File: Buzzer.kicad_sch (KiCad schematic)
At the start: 6 parts, among them Q2 MMBT3904

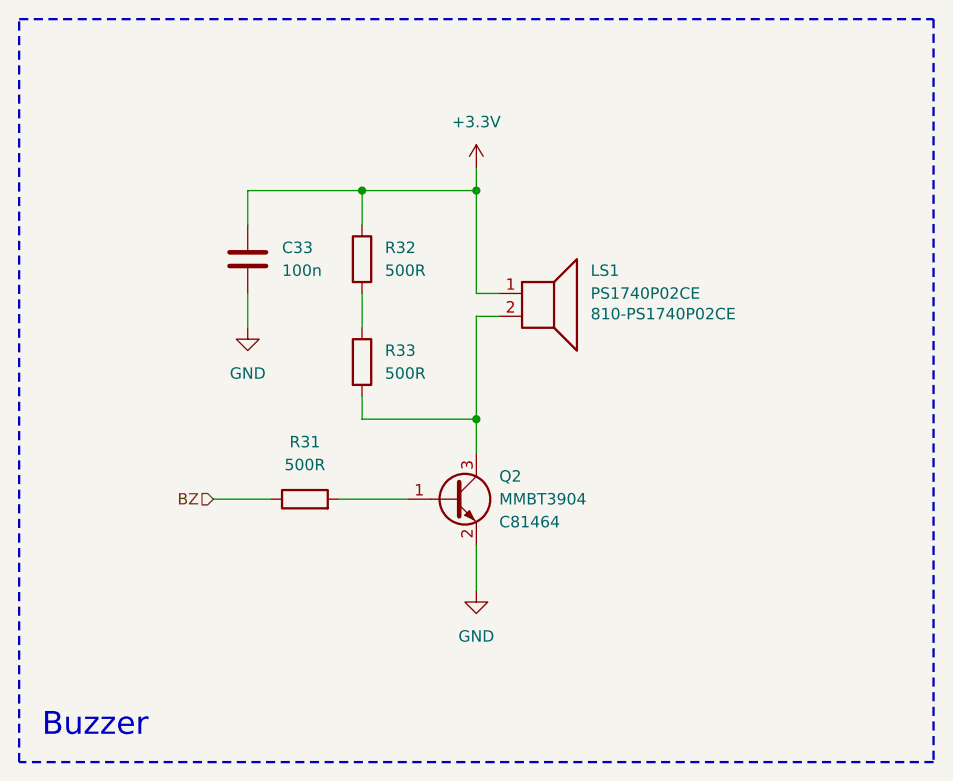
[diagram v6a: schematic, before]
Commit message: display driver update
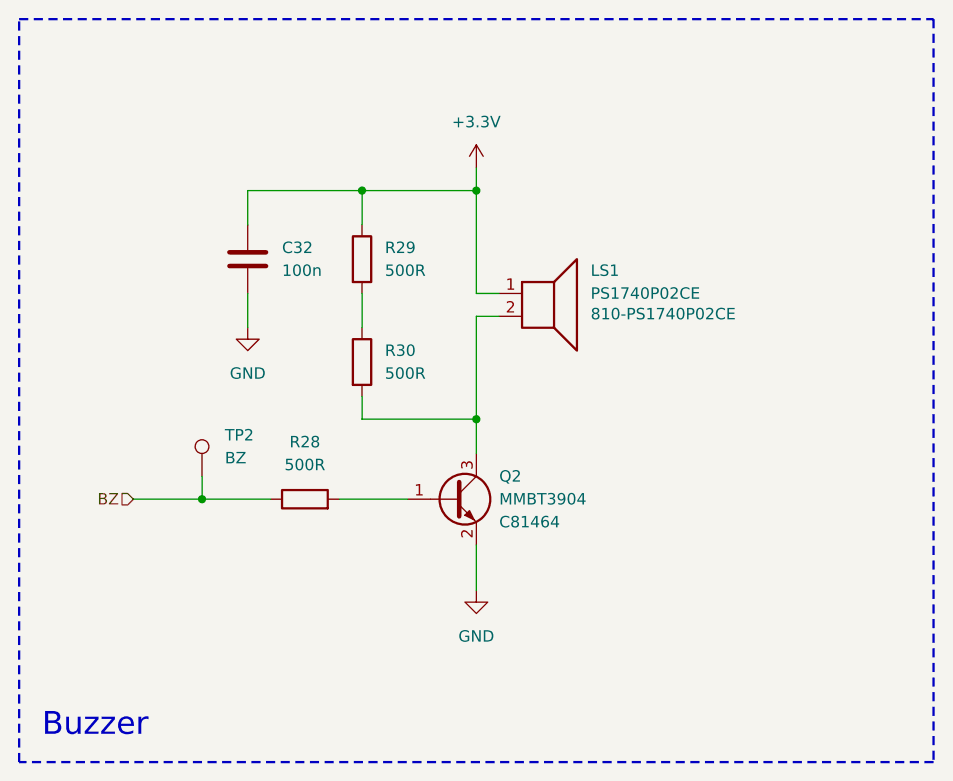
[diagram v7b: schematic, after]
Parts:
- added TP2: BZ, TestPoint:TestPoint_Pad_D1.0mm, symbol Connector:TestPoint
- renumbered C33 to C32, R31 to R28, R32 to R29, R33 to R30
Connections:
- net BZ: now also TP2.1
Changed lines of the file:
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@@
+	)
+	(junction
+		(at 121.92 110.49)
+		(diameter 0)
+		(color 0 0 0 0)
 	)
 	(junction
@@
 	(wire
 		(pts
+			(xy 121.92 107.95) (xy 121.92 110.49)
+		)
+		(stroke
+			(width 0)
+			(type default)
+		)
+	)
+	(wire
+		(pts
 			(xy 154.94 87.63) (xy 152.4 87.63)
 		)
@@
 	(wire
 		(pts
+			(xy 121.92 110.49) (xy 129.54 110.49)
+		)
+		(stroke
+			(width 0)
+			(type default)
+		)
+	)
+	(wire
+		(pts
 			(xy 139.7 87.63) (xy 139.7 91.44)
 		)
@@
 	(wire
 		(pts
-			(xy 123.19 110.49) (xy 129.54 110.49)
+			(xy 114.3 110.49) (xy 121.92 110.49)
 		)
 		(stroke
@@
 	(hierarchical_label "BZ"
 		(shape input)
-		(at 123.19 110.49 180)
+		(at 114.3 110.49 180)
 		(effects
 			(font
@@
 		(on_board yes)
 		(dnp no)
-		(property "Reference" "C33"
+		(property "Reference" "C32"
 			(at 130.81 82.5499 0)
 			(effects
@@
 			(project "Precision Clock"
 				(path "/c9a8ff63-a0d1-4125-9dd1-40fb53daf536/fa1772ae-d612-479d-9fc0-6f13b32ea30c"
-					(reference "C33")
+					(reference "C32")
 					(unit 1)
 				)
@@
 		(dnp no)
 		(fields_autoplaced yes)
-		(property "Reference" "R31"
+		(property "Reference" "R28"
 			(at 133.35 104.14 90)
 			(effects
@@
 			(project ""
 				(path "/c9a8ff63-a0d1-4125-9dd1-40fb53daf536/fa1772ae-d612-479d-9fc0-6f13b32ea30c"
-					(reference "R31")
+					(reference "R28")
+					(unit 1)
+				)
+			)
+		)
+	)
+	(symbol
+		(lib_id "Connector:TestPoint")
+		(at 121.92 107.95 0)
+		(unit 1)
+		(exclude_from_sim no)
+		(in_bom yes)
+		(on_board yes)
+		(dnp no)
+		(fields_autoplaced yes)
+		(property "Reference" "TP2"
+			(at 124.46 103.3779 0)
+			(effects
+				(font
+					(size 1.27 1.27)
+				)
+				(justify left)
+			)
+		)
+		(property "Value" "BZ"
+			(at 124.46 105.9179 0)
+			(effects
+				(font
+					(size 1.27 1.27)
+				)
+				(justify left)
+			)
+		)
+		(property "Footprint" "TestPoint:TestPoint_Pad_D1.0mm"
+			(at 127 107.95 0)
+			(effects
+				(font
+					(size 1.27 1.27)
+				)
+				(hide yes)
+			)
+		)
+		(property "Datasheet" "~"
+			(at 127 107.95 0)
+			(effects
+				(font
+					(size 1.27 1.27)
+				)
+				(hide yes)
+			)
+		)
+		(property "Description" "test point"
+			(at 121.92 107.95 0)
+			(effects
+				(font
+					(size 1.27 1.27)
+				)
+				(hide yes)
+			)
+		)
+		(pin "1"
+		)
+		(instances
+			(project "Precision Clock"
+				(path "/c9a8ff63-a0d1-4125-9dd1-40fb53daf536/fa1772ae-d612-479d-9fc0-6f13b32ea30c"
+					(reference "TP2")
 					(unit 1)
 				)
@@
 		(dnp no)
 		(fields_autoplaced yes)
-		(property "Reference" "R32"
+		(property "Reference" "R29"
 			(at 142.24 82.5499 0)
 			(effects
@@
 			(project "Precision Clock"
 				(path "/c9a8ff63-a0d1-4125-9dd1-40fb53daf536/fa1772ae-d612-479d-9fc0-6f13b32ea30c"
-					(reference "R32")
+					(reference "R29")
 					(unit 1)
 				)
@@
 		(dnp no)
 		(fields_autoplaced yes)
-		(property "Reference" "#PWR087"
+		(property "Reference" "#PWR085"
 			(at 127 97.79 0)
 			(effects
@@
 			(project "Precision Clock"
 				(path "/c9a8ff63-a0d1-4125-9dd1-40fb53daf536/fa1772ae-d612-479d-9fc0-6f13b32ea30c"
-					(reference "#PWR087")
+					(reference "#PWR085")
 					(unit 1)
 				)
@@
 		(dnp no)
 		(fields_autoplaced yes)
-		(property "Reference" "#PWR092"
+		(property "Reference" "#PWR087"
 			(at 152.4 127 0)
 			(effects
@@
 			(project ""
 				(path "/c9a8ff63-a0d1-4125-9dd1-40fb53daf536/fa1772ae-d612-479d-9fc0-6f13b32ea30c"
-					(reference "#PWR092")
+					(reference "#PWR087")
 					(unit 1)
 				)
@@
 		(dnp no)
 		(fields_autoplaced yes)
-		(property "Reference" "#PWR091"
+		(property "Reference" "#PWR086"
 			(at 152.4 77.47 0)
 			(effects
@@
 			(project ""
 				(path "/c9a8ff63-a0d1-4125-9dd1-40fb53daf536/fa1772ae-d612-479d-9fc0-6f13b32ea30c"
-					(reference "#PWR091")
+					(reference "#PWR086")
 					(unit 1)
 				)
@@
 		(dnp no)
 		(fields_autoplaced yes)
-		(property "Reference" "R33"
+		(property "Reference" "R30"
 			(at 142.24 93.9799 0)
 			(effects
@@
 			(project "Precision Clock"
 				(path "/c9a8ff63-a0d1-4125-9dd1-40fb53daf536/fa1772ae-d612-479d-9fc0-6f13b32ea30c"
-					(reference "R33")
+					(reference "R30")
 					(unit 1)
 				)

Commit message: Display Driver Completion
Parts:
- R17: renamed from R28; value 500R -> 510R
- R18: renamed from R29; value 500R -> 510R
- R19: renamed from R30; value 500R -> 510R
- renumbered C32 to C35, TP2 to TP20
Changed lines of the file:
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@@
 	(title_block
 		(title "Buzzer")
-		(date "2026-02-04")
+		(date "2026-02-06")
 		(rev "v0.0")
 		(company "TJ71PL")
@@
 		(on_board yes)
 		(dnp no)
-		(property "Reference" "C32"
+		(property "Reference" "C35"
 			(at 130.81 82.5499 0)
 			(effects
@@
 			(project "Precision Clock"
 				(path "/c9a8ff63-a0d1-4125-9dd1-40fb53daf536/fa1772ae-d612-479d-9fc0-6f13b32ea30c"
-					(reference "C32")
+					(reference "C35")
 					(unit 1)
 				)
@@
 	)
 	(symbol
+		(lib_name "MMBT3904_1")
 		(lib_id "Transistor_BJT:MMBT3904")
 		(at 149.86 110.49 0)
@@
 		(dnp no)
 		(property "Reference" "Q2"
-			(at 154.94 107.9501 0)
+			(at 154.94 107.95 0)
 			(effects
 				(font
@@
 			)
 		)
+		(property "Sim.Device" "NPN"
+			(at 149.86 110.49 0)
+			(effects
+				(font
+					(size 1.27 1.27)
+				)
+				(hide yes)
+			)
+		)
+		(property "Sim.Pins" "1=B 2=E 3=C"
+			(at 149.86 110.49 0)
+			(effects
+				(font
+					(size 1.27 1.27)
+				)
+				(hide yes)
+			)
+		)
 		(property "LCSC" "C81464"
 			(at 154.94 113.0301 0)
@@
 			)
 		)
+		(pin "1"
+		)
+		(pin "3"
+		)
 		(pin "2"
-		)
-		(pin "1"
-		)
-		(pin "3"
 		)
 		(instances
@@
 		(dnp no)
 		(fields_autoplaced yes)
-		(property "Reference" "R28"
+		(property "Reference" "R17"
 			(at 133.35 104.14 90)
 			(effects
@@
 			)
 		)
-		(property "Value" "500R"
+		(property "Value" "510R"
 			(at 133.35 106.68 90)
 			(effects
@@
 			(project ""
 				(path "/c9a8ff63-a0d1-4125-9dd1-40fb53daf536/fa1772ae-d612-479d-9fc0-6f13b32ea30c"
-					(reference "R28")
+					(reference "R17")
 					(unit 1)
 				)
@@
 		(dnp no)
 		(fields_autoplaced yes)
-		(property "Reference" "TP2"
+		(property "Reference" "TP20"
 			(at 124.46 103.3779 0)
 			(effects
@@
 			(project "Precision Clock"
 				(path "/c9a8ff63-a0d1-4125-9dd1-40fb53daf536/fa1772ae-d612-479d-9fc0-6f13b32ea30c"
-					(reference "TP2")
+					(reference "TP20")
 					(unit 1)
 				)
@@
 		(dnp no)
 		(fields_autoplaced yes)
-		(property "Reference" "R29"
+		(property "Reference" "R18"
 			(at 142.24 82.5499 0)
 			(effects
@@
 			)
 		)
-		(property "Value" "500R"
+		(property "Value" "510R"
 			(at 142.24 85.0899 0)
 			(effects
@@
 			(project "Precision Clock"
 				(path "/c9a8ff63-a0d1-4125-9dd1-40fb53daf536/fa1772ae-d612-479d-9fc0-6f13b32ea30c"
-					(reference "R29")
+					(reference "R18")
 					(unit 1)
 				)
@@
 		(dnp no)
 		(fields_autoplaced yes)
-		(property "Reference" "#PWR085"
+		(property "Reference" "#PWR092"
 			(at 127 97.79 0)
 			(effects
@@
 			(project "Precision Clock"
 				(path "/c9a8ff63-a0d1-4125-9dd1-40fb53daf536/fa1772ae-d612-479d-9fc0-6f13b32ea30c"
-					(reference "#PWR085")
+					(reference "#PWR092")
 					(unit 1)
 				)
@@
 		(dnp no)
 		(fields_autoplaced yes)
-		(property "Reference" "#PWR087"
+		(property "Reference" "#PWR094"
 			(at 152.4 127 0)
 			(effects
@@
 			(project ""
 				(path "/c9a8ff63-a0d1-4125-9dd1-40fb53daf536/fa1772ae-d612-479d-9fc0-6f13b32ea30c"
-					(reference "#PWR087")
+					(reference "#PWR094")
 					(unit 1)
 				)
@@
 		(dnp no)
 		(fields_autoplaced yes)
-		(property "Reference" "#PWR086"
+		(property "Reference" "#PWR093"
 			(at 152.4 77.47 0)
 			(effects
@@
 			(project ""
 				(path "/c9a8ff63-a0d1-4125-9dd1-40fb53daf536/fa1772ae-d612-479d-9fc0-6f13b32ea30c"
-					(reference "#PWR086")
+					(reference "#PWR093")
 					(unit 1)
 				)
@@
 		(dnp no)
 		(fields_autoplaced yes)
-		(property "Reference" "R30"
+		(property "Reference" "R19"
 			(at 142.24 93.9799 0)
 			(effects
@@
 			)
 		)
-		(property "Value" "500R"
+		(property "Value" "510R"
 			(at 142.24 96.5199 0)
 			(effects
@@
 			(project "Precision Clock"
 				(path "/c9a8ff63-a0d1-4125-9dd1-40fb53daf536/fa1772ae-d612-479d-9fc0-6f13b32ea30c"
-					(reference "R30")
+					(reference "R19")
 					(unit 1)
 				)
